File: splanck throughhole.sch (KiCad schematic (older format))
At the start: 51 parts, among them K1 XLR3, SW1 SW_PUSH, SW10 SW_PUSH, SW11 SW_PUSH, SW12 SW_PUSH, SW13 SW_PUSH, SW14 SW_PUSH, SW15 SW_PUSH, SW16 SW_PUSH, SW17 SW_PUSH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

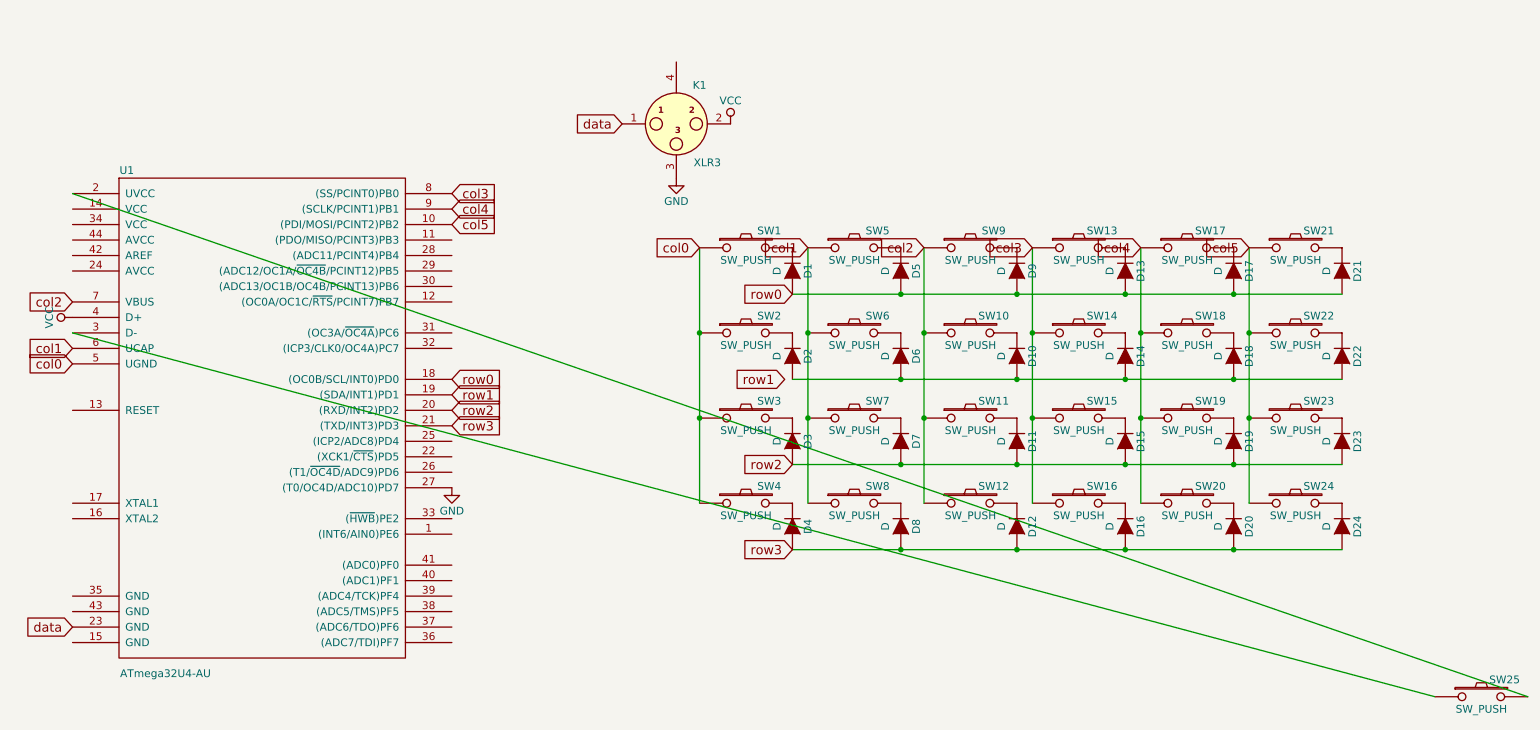
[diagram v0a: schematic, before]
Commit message: brought the pcb up to date and fixed reset pin
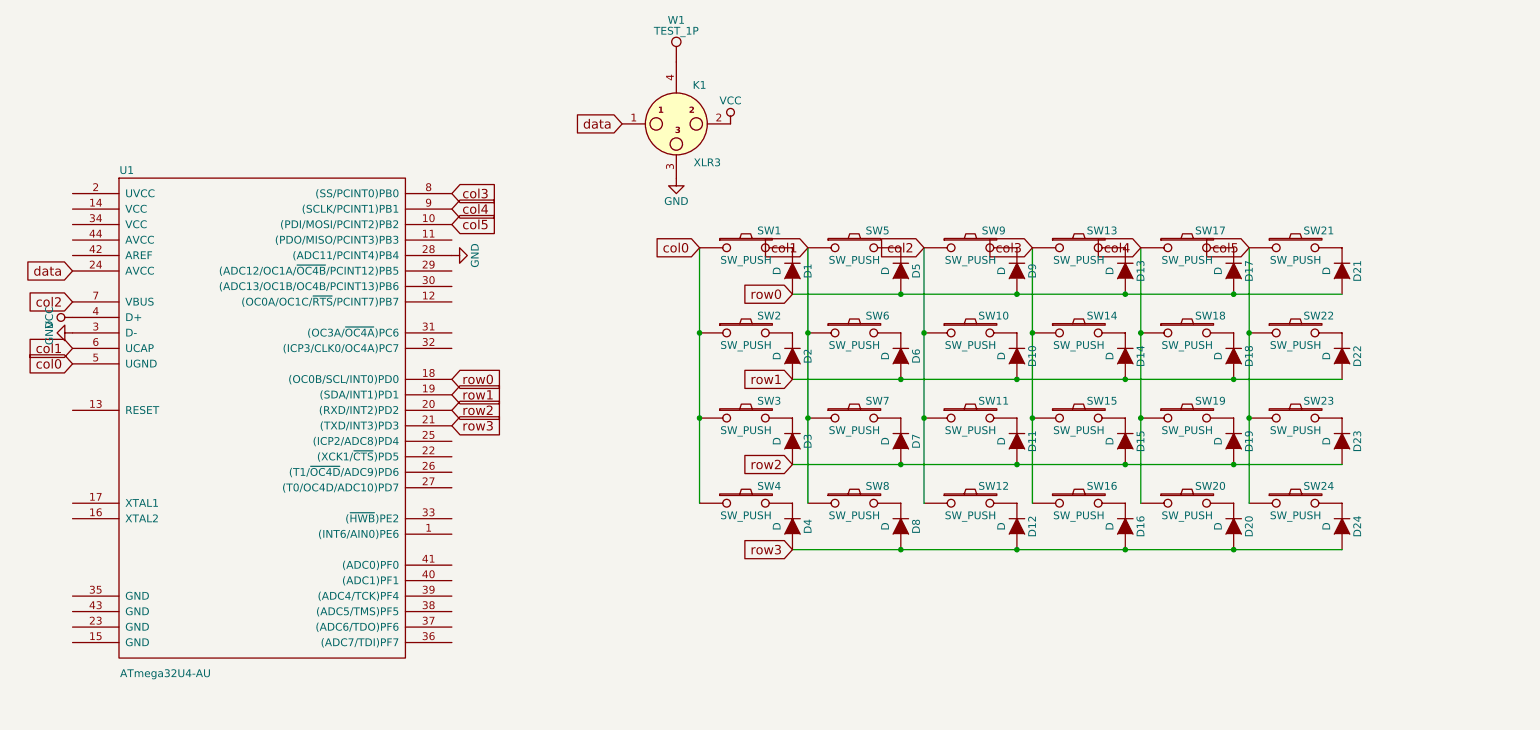
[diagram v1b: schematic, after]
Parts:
- removed SW25: SW_PUSH, Buttons_Switches_SMD:SW_SPST_FSMSM, symbol SW_PUSH
- added W1: TEST_1P, Wire_Pads:SolderWirePad_single_0-8mmDrill, symbol TEST_1P
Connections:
- net GND: now also U1.28 ((ADC11/PCINT4)PB4), U1.3 (D-); no longer U1.27 ((T0/OC4D/ADC10)PD7)
- net data: now also U1.24 (AVCC); no longer U1.23 (GND)
- net row1: now also D10.2 (A), D14.2 (A), D18.2 (A), D2.2 (A), D22.2 (A), D6.2 (A)
- net at K1.4: now also W1.1
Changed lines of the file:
@@
 LIBS:contrib
 LIBS:valves
+LIBS:splanck throughhole-cache
 EELAYER 25 0
 EELAYER END
@@
 Text GLabel 5850 2350 0    60   Input ~ 0
 row0
-Text GLabel 5800 2900 0    60   Input ~ 0
+Text GLabel 5850 2900 0    60   Input ~ 0
 row1
 Text GLabel 5850 4000 0    60   Input ~ 0
@@
 Text GLabel 3650 3200 2    60   Input ~ 0
 row3
-Text GLabel 1200 4500 0    60   Input ~ 0
+Text GLabel 1200 2200 0    60   Input ~ 0
 data
 $Comp
@@
 $EndComp
 $Comp
-L SW_PUSH SW25
-U 1 1 574BD152
-P 10300 4950
-F 0 "SW25" H 10450 5060 50  0000 C CNN
-F 1 "SW_PUSH" H 10300 4870 50  0000 C CNN
-F 2 "Buttons_Switches_SMD:SW_SPST_FSMSM" H 10300 4950 50  0001 C CNN
-F 3 "" H 10300 4950 50  0000 C CNN
-	1    10300 4950
-	1    0    0    -1
-$EndComp
-Wire Wire Line
-	1200 1700 10600 4950
-Wire Wire Line
-	1200 2600 10000 4950
-$Comp
 L GND #PWR01
 U 1 1 574BF981
-P 3650 3600
-F 0 "#PWR01" H 3650 3350 50  0001 C CNN
-F 1 "GND" H 3650 3450 50  0000 C CNN
-F 2 "" H 3650 3600 50  0000 C CNN
-F 3 "" H 3650 3600 50  0000 C CNN
-	1    3650 3600
-	1    0    0    -1
+P 3650 2100
+F 0 "#PWR01" H 3650 1850 50  0001 C CNN
+F 1 "GND" H 3650 1950 50  0000 C CNN
+F 2 "" H 3650 2100 50  0000 C CNN
+F 3 "" H 3650 2100 50  0000 C CNN
+	1    3650 2100
+	0    -1   -1   0
 $EndComp
 $Comp
@@
 Text GLabel 4750 1250 0    60   Input ~ 0
 data
+$Comp
+L TEST_1P W1
+U 1 1 576620E6
+P 5100 850
+F 0 "W1" H 5100 1120 50  0000 C CNN
+F 1 "TEST_1P" H 5100 1050 50  0000 C CNN
+F 2 "Wire_Pads:SolderWirePad_single_0-8mmDrill" H 5300 850 50  0001 C CNN
+F 3 "" H 5300 850 50  0000 C CNN
+	1    5100 850
+	1    0    0    -1
+$EndComp
+$Comp
+L GND #PWR?
+U 1 1 576655BB
+P 1200 2600
+F 0 "#PWR?" H 1200 2350 50  0001 C CNN
+F 1 "GND" H 1200 2450 50  0000 C CNN
+F 2 "" H 1200 2600 50  0000 C CNN
+F 3 "" H 1200 2600 50  0000 C CNN
+	1    1200 2600
+	0    1    1    0
+$EndComp
 $EndSCHEMATC
